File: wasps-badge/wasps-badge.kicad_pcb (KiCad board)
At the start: 2 copper layers, 75 x 75 mm, 24 parts, among them J1 Conn_Debug, J2 Conn_AddOn, J3 Conn_CTF, SW1 SW_SPDT, SW2 SW_Push, SW3 SW_Push, U1 CH32V003FxPx

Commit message: Define resistor values
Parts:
- R2, R5: value R -> 20k
- R3, R4: value R -> 2.2k
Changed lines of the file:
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@@
 	(net 29 "unconnected-(U1-PA1-Pad5)")
 	(net 30 "/VBAT")
-	(net 31 "unconnected-(SW1-A-Pad1)_1")
+	(net 31 "unconnected-(SW1-A-Pad1)")
 	(footprint "Resistor_SMD:R_0603_1608Metric_Pad0.98x0.95mm_HandSolder"
 		(layer "F.Cu")
@@
 			)
 		)
-		(property "Value" "R"
+		(property "Value" "2.2k"
 			(at 0 1.43 45)
 			(layer "F.Fab")
@@
 			)
 		)
-		(property "Value" "R"
+		(property "Value" "20k"
 			(at 0 1.43 45)
 			(layer "F.Fab")
@@
 			)
 		)
-		(property "Value" "R"
+		(property "Value" "2.2k"
 			(at 0 1.43 45)
 			(layer "F.Fab")
@@
 			)
 		)
-		(attr board_only)
+		(attr board_only exclude_from_pos_files exclude_from_bom)
 		(fp_poly
 			(pts
@@
 			)
 		)
-		(property "Value" "R"
+		(property "Value" "20k"
 			(at 0 1.43 45)
 			(layer "F.Fab")
@@
 			(size 1.1 1.95)
 			(layers "B.Cu" "B.Mask" "B.Paste")
-			(net 31 "unconnected-(SW1-A-Pad1)_1")
+			(net 31 "unconnected-(SW1-A-Pad1)")
 			(pinfunction "A")
 			(pintype "passive+no_connect")
@@
 			(size 1.1 1.95)
 			(layers "B.Cu" "B.Mask" "B.Paste")
-			(net 31 "unconnected-(SW1-A-Pad1)_1")
+			(net 31 "unconnected-(SW1-A-Pad1)")
 			(pinfunction "A")
 			(pintype "passive+no_connect")

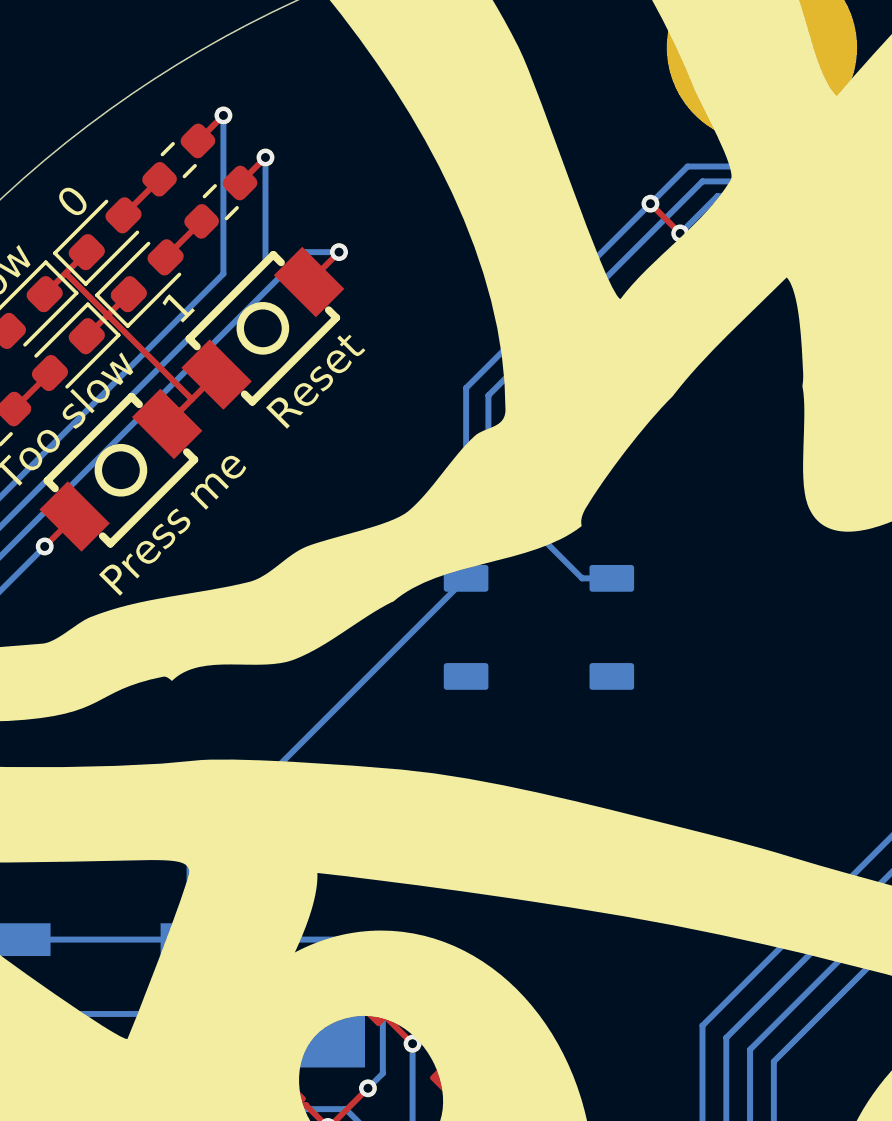
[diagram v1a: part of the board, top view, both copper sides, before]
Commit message: Tweak LED5 location
Maybe placing a raised ground pin close to... any of the battery's
contacts is not *that* good an idea.
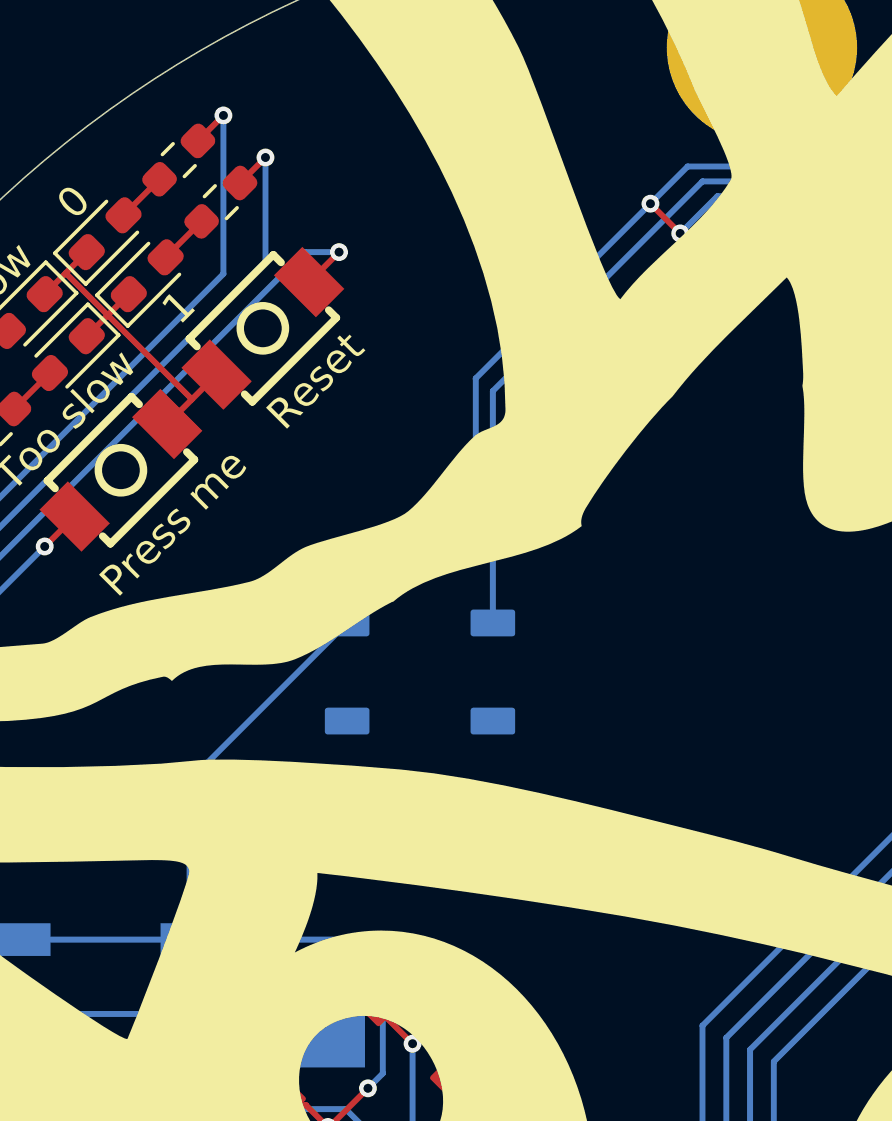
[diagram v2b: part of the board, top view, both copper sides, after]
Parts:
- moved LED5 4.27 mm to (88.5, 88.5)
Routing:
- net Net-(LED4-DOUT): track 73.8 -> 73.0 mm
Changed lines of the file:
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@@
 	(footprint "CustomLibrary:LED_WS2812B_Reverse"
 		(layer "B.Cu")
-		(at 92.5 87)
+		(at 88.5 88.5)
 		(descr "5.0mm x 5.0mm Addressable RGB LED NeoPixel, Reverse-mounted, https://cdn-shop.adafruit.com/datasheets/WS2812B.pdf")
 		(tags "LED RGB NeoPixel PLCC-4 5050")
@@
 				(pts
 					(arc
-						(start 90.5 87)
-						(mid 94.5 87)
-						(end 90.5 87)
+						(start 86.5 88.5)
+						(mid 90.5 88.5)
+						(end 86.5 88.5)
 					)
 				)
@@
 	)
 	(via
-		(at 86.5 85)
+		(at 86.25 85.125)
 		(size 0.6)
 		(drill 0.3)
@@
 	)
 	(via
-		(at 81.5 92.25)
+		(at 81.875 92.5)
 		(size 0.6)
 		(drill 0.3)
@@
 	)
 	(segment
-		(start 80.75 97.5)
-		(end 80.75 94.65)
-		(width 0.2)
-		(layer "B.Cu")
-		(net 2)
-	)
-	(segment
 		(start 127.901 78.4161)
 		(end 124.9161 81.401)
@@
 	)
 	(segment
+		(start 90.375 82.525)
+		(end 90.375 78.625)
+		(width 0.2)
+		(layer "B.Cu")
+		(net 2)
+	)
+	(segment
 		(start 102.95 117.35)
 		(end 101.75 118.55)
@@
 	)
 	(segment
-		(start 80.75 94.65)
-		(end 90.05 85.35)
-		(width 0.2)
-		(layer "B.Cu")
-		(net 2)
-	)
-	(segment
 		(start 87.25 102)
 		(end 87.25 98)
@@
 	)
 	(segment
-		(start 96.25 72.75)
-		(end 90.05 78.95)
+		(start 80.75 92.15)
+		(end 90.375 82.525)
 		(width 0.2)
 		(layer "B.Cu")
@@
 	)
 	(segment
+		(start 90.375 78.625)
+		(end 96.25 72.75)
+		(width 0.2)
+		(layer "B.Cu")
+		(net 2)
+	)
+	(segment
 		(start 124.9161 81.401)
 		(end 122.999 81.401)
@@
 	)
 	(segment
-		(start 90.05 78.95)
-		(end 90.05 85.35)
+		(start 124.75 89.5)
+		(end 119.4 89.5)
 		(width 0.2)
 		(layer "B.Cu")
@@
 	)
 	(segment
-		(start 124.75 89.5)
-		(end 119.4 89.5)
+		(start 80.75 97.5)
+		(end 80.75 92.15)
 		(width 0.2)
 		(layer "B.Cu")
@@
 	)
 	(segment
-		(start 116.6 91.7)
-		(end 116.6 86.6)
+		(start 90.95 79.05)
+		(end 90.95 86.85)
 		(width 0.2)
 		(layer "B.Cu")
@@
 	)
 	(segment
-		(start 127.5 76.75)
-		(end 122.75 72)
+		(start 118.55 93.65)
+		(end 116.6 91.7)
 		(width 0.2)
 		(layer "B.Cu")
@@
 	)
 	(segment
-		(start 90.8 79.2)
-		(end 90.8 82.2)
+		(start 127.5 78.25)
+		(end 127.5 76.75)
 		(width 0.2)
 		(layer "B.Cu")
@@
 	)
 	(segment
-		(start 124.95 80.8)
-		(end 127.5 78.25)
+		(start 98 72)
+		(end 90.95 79.05)
 		(width 0.2)
 		(layer "B.Cu")
@@
 	)
 	(segment
-		(start 122.75 72)
-		(end 98 72)
+		(start 116.6 91.7)
+		(end 116.6 86.6)
 		(width 0.2)
 		(layer "B.Cu")
@@
 	)
 	(segment
-		(start 116.6 86.6)
-		(end 122.4 80.8)
+		(start 127.5 76.75)
+		(end 122.75 72)
 		(width 0.2)
 		(layer "B.Cu")
@@
 	)
 	(segment
-		(start 118.55 93.65)
-		(end 116.6 91.7)
+		(start 116.6 86.6)
+		(end 122.4 80.8)
 		(width 0.2)
 		(layer "B.Cu")
@@
 	)
 	(segment
-		(start 127.5 78.25)
-		(end 127.5 76.75)
-		(width 0.2)
-		(layer "B.Cu")
-		(net 25)
-	)
-	(segment
-		(start 98 72)
-		(end 90.8 79.2)
-		(width 0.2)
-		(layer "B.Cu")
-		(net 25)
-	)
-	(segment
-		(start 90.8 82.2)
-		(end 93.95 85.35)
+		(start 122.75 72)
+		(end 98 72)
 		(width 0.2)
 		(layer "B.Cu")
@@
 	)
 	(segment
-		(start 93.95 85.35)
-		(end 94.95 85.35)
+		(start 124.95 80.8)
+		(end 127.5 78.25)
 		(width 0.2)
 		(layer "B.Cu")

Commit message: Add supplier part numbers
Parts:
- LED1, LED2: value WS2812B_MINI -> WS2812B
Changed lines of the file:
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@@
 			)
 		)
+		(property "LCSC" "C4190"
+			(at 0 0 0)
+			(layer "F.SilkS")
+			(hide yes)
+			(effects
+				(font
+					(size 1.27 1.27)
+					(thickness 0.15)
+				)
+			)
+		)
 		(property ki_fp_filters "R_*")
 		(sheetname "/")
@@
 			)
 		)
+		(property "LCSC" "C5116527"
+			(at 0 0 0)
+			(layer "F.SilkS")
+			(hide yes)
+			(effects
+				(font
+					(size 1.27 1.27)
+					(thickness 0.15)
+				)
+			)
+		)
 		(property ki_fp_filters "Connector*:*_2x??_*")
 		(sheetname "/")
@@
 			)
 		)
+		(property "LCSC" "C5221275"
+			(at 0 0 0)
+			(layer "F.SilkS")
+			(hide yes)
+			(effects
+				(font
+					(size 1.27 1.27)
+					(thickness 0.15)
+				)
+			)
+		)
 		(sheetname "/")
 		(sheetfile "wasps-badge.kicad_sch")
@@
 			)
 		)
+		(property "LCSC" "C4184"
+			(at 0 0 0)
+			(layer "F.SilkS")
+			(hide yes)
+			(effects
+				(font
+					(size 1.27 1.27)
+					(thickness 0.15)
+				)
+			)
+		)
 		(property ki_fp_filters "R_*")
 		(sheetname "/")
@@
 			)
 		)
+		(property "LCSC" "C4190"
+			(at 0 0 0)
+			(layer "F.SilkS")
+			(hide yes)
+			(effects
+				(font
+					(size 1.27 1.27)
+					(thickness 0.15)
+				)
+			)
+		)
 		(property ki_fp_filters "R_*")
 		(sheetname "/")
@@
 			)
 		)
+		(property "LCSC" "C965799"
+			(at 0 0 0)
+			(layer "F.SilkS")
+			(hide yes)
+			(effects
+				(font
+					(size 1.27 1.27)
+					(thickness 0.15)
+				)
+			)
+		)
 		(property ki_fp_filters "LED* LED_SMD:* LED_THT:*")
 		(sheetname "/")
@@
 			)
 		)
+		(property "LCSC" "C5221275"
+			(at 0 0 0)
+			(layer "F.SilkS")
+			(hide yes)
+			(effects
+				(font
+					(size 1.27 1.27)
+					(thickness 0.15)
+				)
+			)
+		)
 		(sheetname "/")
 		(sheetfile "wasps-badge.kicad_sch")
@@
 			)
 		)
+		(property "LCSC" "C12624"
+			(at 0 0 0)
+			(layer "F.SilkS")
+			(hide yes)
+			(effects
+				(font
+					(size 1.27 1.27)
+					(thickness 0.15)
+				)
+			)
+		)
 		(property ki_fp_filters "LED* LED_SMD:* LED_THT:*")
 		(sheetname "/")
@@
 			)
 		)
-		(property "Value" "WS2812B_MINI"
+		(property "Value" "WS2812B"
 			(at 0 4 45)
 			(layer "F.Fab")
@@
 			)
 		)
+		(property "LCSC" "C2874885"
+			(at 0 0 0)
+			(layer "F.SilkS")
+			(hide yes)
+			(effects
+				(font
+					(size 1.27 1.27)
+					(thickness 0.15)
+				)
+			)
+		)
 		(property ki_fp_filters "LED*WS2812*PLCC*5.0x5.0mm*P3.2mm*")
 		(sheetname "/")
@@
 			)
 		)
+		(property "LCSC" "C12624"
+			(at 0 0 0)
+			(layer "F.SilkS")
+			(hide yes)
+			(effects
+				(font
+					(size 1.27 1.27)
+					(thickness 0.15)
+				)
+			)
+		)
 		(property ki_fp_filters "LED* LED_SMD:* LED_THT:*")
 		(sheetname "/")
@@
 			)
 		)
-		(property "Value" "WS2812B_MINI"
+		(property "Value" "WS2812B"
 			(at 0 4 45)
 			(layer "F.Fab")
@@
 			)
 		)
+		(property "LCSC" "C2874885"
+			(at 0 0 0)
+			(layer "F.SilkS")
+			(hide yes)
+			(effects
+				(font
+					(size 1.27 1.27)
+					(thickness 0.15)
+				)
+			)
+		)
 		(property ki_fp_filters "LED*WS2812*PLCC*5.0x5.0mm*P3.2mm*")
 		(sheetname "/")
@@
 			)
 		)
+		(property "LCSC" "C965799"
+			(at 0 0 0)
+			(layer "F.SilkS")
+			(hide yes)
+			(effects
+				(font
+					(size 1.27 1.27)
+					(thickness 0.15)
+				)
+			)
+		)
 		(property ki_fp_filters "LED* LED_SMD:* LED_THT:*")
 		(sheetname "/")
@@
 			)
 		)
+		(property "LCSC" "C4184"
+			(at 0 0 0)
+			(layer "F.SilkS")
+			(hide yes)
+			(effects
+				(font
+					(size 1.27 1.27)
+					(thickness 0.15)
+				)
+			)
+		)
 		(property ki_fp_filters "R_*")
 		(sheetname "/")
@@
 			)
 		)
+		(property "LCSC" "C2874885"
+			(at 0 0 0)
+			(layer "B.SilkS")
+			(hide yes)
+			(effects
+				(font
+					(size 1.27 1.27)
+					(thickness 0.15)
+				)
+			)
+		)
 		(property ki_fp_filters "LED*WS2812*PLCC*5.0x5.0mm*P3.2mm*")
 		(sheetname "/")
@@
 			)
 		)
+		(property "LCSC" "C19702"
+			(at 0 0 0)
+			(layer "B.SilkS")
+			(hide yes)
+			(effects
+				(font
+					(size 1.27 1.27)
+					(thickness 0.15)
+				)
+			)
+		)
 		(property ki_fp_filters "C_*")
 		(sheetname "/")
@@
 			)
 		)
+		(property "LCSC" "C2874885"
+			(at 0 0 0)
+			(layer "B.SilkS")
+			(hide yes)
+			(effects
+				(font
+					(size 1.27 1.27)
+					(thickness 0.15)
+				)
+			)
+		)
 		(property ki_fp_filters "LED*WS2812*PLCC*5.0x5.0mm*P3.2mm*")
 		(sheetname "/")
@@
 			)
 		)
+		(property "LCSC" "C5187096"
+			(at 0 0 0)
+			(layer "B.SilkS")
+			(hide yes)
+			(effects
+				(font
+					(size 1.27 1.27)
+					(thickness 0.15)
+				)
+			)
+		)
 		(property ki_fp_filters "TSSOP*4.4x6.5mm*P0.65mm*")
 		(sheetname "/")
@@
 			)
 		)
+		(property "LCSC" "C2874885"
+			(at 0 0 0)
+			(layer "B.SilkS")
+			(hide yes)
+			(effects
+				(font
+					(size 1.27 1.27)
+					(thickness 0.15)
+				)
+			)
+		)
 		(property ki_fp_filters "LED*WS2812*PLCC*5.0x5.0mm*P3.2mm*")
 		(sheetname "/")
@@
 			)
 		)
+		(property "LCSC" "C70377"
+			(at 0 0 0)
+			(layer "B.SilkS")
+			(hide yes)
+			(effects
+				(font
+					(size 1.27 1.27)
+					(thickness 0.15)
+				)
+			)
+		)
 		(sheetname "/")
 		(sheetfile "wasps-badge.kicad_sch")
@@
 					(thickness 0.15)
 				)
+				(justify mirror)
+			)
+		)
+		(property "LCSC" "C41375971"
+			(at 0 0 90)
+			(unlocked yes)
+			(layer "B.Fab")
+			(hide yes)
+			(effects
+				(font
+					(size 1 1)
+					(thickness 0.15)
+				)
